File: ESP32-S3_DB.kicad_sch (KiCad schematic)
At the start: 0 parts

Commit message: Started ESP routing
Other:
- sheet CAN TRANSCEIVER ports: added CAN_N, CAN_P; removed CAN_H, CAN_L
- sheet ESP32-S3 ports: added none; removed GPIO15, GPIO16
- sheet EXTERNAL CONNECTORS ports: added CAN_N, CAN_P, RS485_N, RS485_P; removed CAN_H, CAN_L, GPIO15, GPIO16, RS-485_A, RS-485_B
- sheet RS_485 ports: added RS485_N, RS485_P; removed RS_485_A, RS_485_B
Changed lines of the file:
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@@
     (stroke (width 0.5) (type default) (color 0 0 255 1))
-  )
-  (wire (pts (xy 259.715 123.825) (xy 276.225 123.825))
-    (stroke (width 0.5) (type default) (color 72 0 72 1))
   )
   (wire (pts (xy 199.39 85.725) (xy 220.345 85.725))
@@
     (stroke (width 0.5) (type default) (color 0 0 255 1))
   )
-  (wire (pts (xy 165.735 110.49) (xy 174.625 110.49))
-    (stroke (width 0.5) (type default) (color 72 0 72 1))
-  )
   (polyline (pts (xy 88.9 147.32) (xy 88.9 61.595))
     (stroke (width 0.4) (type dash) (color 0 0 0 1))
   )
-  (wire (pts (xy 259.715 121.285) (xy 276.225 121.285))
-    (stroke (width 0.5) (type default) (color 72 0 72 1))
-  )
   (wire (pts (xy 212.725 37.465) (xy 227.965 37.465))
     (stroke (width 0.5) (type default) (color 204 102 0 1))
@@
   )
   (wire (pts (xy 220.345 93.345) (xy 199.39 93.345))
-    (stroke (width 0.5) (type default) (color 72 0 72 1))
-  )
-  (wire (pts (xy 165.735 107.95) (xy 174.625 107.95))
     (stroke (width 0.5) (type default) (color 72 0 72 1))
   )
@@
     (effects (font (size 1.27 1.27) bold (color 72 0 72 1)) (justify left bottom))
   )
-  (label "RS_485_B" (at 276.225 83.185 180) (fields_autoplaced)
+  (label "RS485_N" (at 276.225 83.185 180) (fields_autoplaced)
     (effects (font (size 1.27 1.27) bold (color 0 0 0 1)) (justify right bottom))
   )
@@
     (effects (font (size 1.27 1.27) bold (color 72 0 72 1)) (justify left bottom))
   )
-  (label "GPIO16" (at 174.625 107.95 180) (fields_autoplaced)
-    (effects (font (size 1.27 1.27) bold (color 72 0 72 1)) (justify right bottom))
-  )
   (label "GPIO3" (at 276.225 106.045 180) (fields_autoplaced)
     (effects (font (size 1.27 1.27) bold (color 72 0 72 1)) (justify right bottom))
@@
     (effects (font (size 1.27 1.27) bold (color 132 132 0 1)) (justify left bottom))
   )
-  (label "GPIO16" (at 276.225 123.825 180) (fields_autoplaced)
-    (effects (font (size 1.27 1.27) bold (color 72 0 72 1)) (justify right bottom))
-  )
   (label "U2U_CONN_TX" (at 95.885 174.625 180) (fields_autoplaced)
     (effects (font (size 1.27 1.27) (thickness 0.254) bold (color 0 0 255 1)) (justify right bottom))
@@
     (effects (font (size 1.27 1.27) bold (color 132 0 0 1)) (justify left bottom))
   )
-  (label "RS_485_B" (at 23.495 84.455 0) (fields_autoplaced)
+  (label "RS485_N" (at 23.495 84.455 0) (fields_autoplaced)
     (effects (font (size 1.27 1.27) bold (color 0 0 0 1)) (justify left bottom))
   )
@@
     (effects (font (size 1.27 1.27) bold (color 72 0 72 1)) (justify right bottom))
   )
-  (label "RS_485_A" (at 23.495 81.915 0) (fields_autoplaced)
+  (label "RS485_P" (at 23.495 81.915 0) (fields_autoplaced)
     (effects (font (size 1.27 1.27) bold (color 0 0 0 1)) (justify left bottom))
   )
@@
   (label "R4_~{RE}_DE" (at 199.39 111.125 0) (fields_autoplaced)
     (effects (font (size 1.27 1.27) bold (color 72 0 72 1)) (justify left bottom))
-  )
-  (label "GPIO15" (at 174.625 110.49 180) (fields_autoplaced)
-    (effects (font (size 1.27 1.27) bold (color 72 0 72 1)) (justify right bottom))
   )
   (label "BOOT" (at 97.155 114.3 0) (fields_autoplaced)
@@
     (effects (font (size 1.27 1.27) bold (color 0 0 255 1)) (justify left bottom))
   )
-  (label "CAN_H" (at 276.225 85.725 180) (fields_autoplaced)
+  (label "CAN_P" (at 276.225 85.725 180) (fields_autoplaced)
     (effects (font (size 1.27 1.27) bold (color 0 0 0 1)) (justify right bottom))
   )
-  (label "CAN_L" (at 276.225 88.265 180) (fields_autoplaced)
+  (label "CAN_N" (at 276.225 88.265 180) (fields_autoplaced)
     (effects (font (size 1.27 1.27) bold (color 0 0 0 1)) (justify right bottom))
   )
@@
     (effects (font (size 1.27 1.27) bold (color 0 0 255 1)) (justify right bottom))
   )
-  (label "RS_485_A" (at 276.225 80.645 180) (fields_autoplaced)
+  (label "RS485_P" (at 276.225 80.645 180) (fields_autoplaced)
     (effects (font (size 1.27 1.27) bold (color 0 0 0 1)) (justify right bottom))
   )
@@
     (effects (font (size 1.27 1.27) bold (color 0 194 0 1)) (justify left bottom))
   )
-  (label "CAN_H" (at 30.48 125.095 0) (fields_autoplaced)
+  (label "CAN_P" (at 30.48 125.095 0) (fields_autoplaced)
     (effects (font (size 1.27 1.27) bold (color 0 0 0 1)) (justify left bottom))
-  )
-  (label "GPIO15" (at 276.225 121.285 180) (fields_autoplaced)
-    (effects (font (size 1.27 1.27) bold (color 72 0 72 1)) (justify right bottom))
   )
   (label "U2U_TXD" (at 181.61 34.925 180) (fields_autoplaced)
@@
     (effects (font (size 1.27 1.27) bold (color 72 0 72 1)) (justify right bottom))
   )
-  (label "CAN_L" (at 30.48 122.555 0) (fields_autoplaced)
+  (label "CAN_N" (at 30.48 122.555 0) (fields_autoplaced)
     (effects (font (size 1.27 1.27) bold (color 0 0 0 1)) (justify left bottom))
   )
@@
       (effects (font (size 1.27 1.27)) (justify left top) hide)
     )
-    (pin "CAN_L" input (at 40.005 122.555 180)
+    (pin "CAN_N" input (at 40.005 122.555 180)
       (effects (font (size 1.27 1.27) (thickness 0.254) bold (color 0 0 0 1)) (justify left))
     )
@@
       (effects (font (size 1.27 1.27) (thickness 0.254) bold (color 255 0 0 1)) (justify right))
     )
-    (pin "CAN_H" input (at 40.005 125.095 180)
+    (pin "CAN_P" input (at 40.005 125.095 180)
       (effects (font (size 1.27 1.27) (thickness 0.254) bold (color 0 0 0 1)) (justify left))
     )
@@
       (effects (font (size 1.27 1.27) (thickness 0.254) bold (color 0 194 0 1)) (justify left))
     )
-    (pin "RS_485_A" bidirectional (at 40.005 81.915 180)
+    (pin "RS485_P" bidirectional (at 40.005 81.915 180)
       (effects (font (size 1.27 1.27) (thickness 0.254) bold (color 0 0 0 1)) (justify left))
     )
-    (pin "RS_485_B" bidirectional (at 40.005 84.455 180)
+    (pin "RS485_N" bidirectional (at 40.005 84.455 180)
       (effects (font (size 1.27 1.27) (thickness 0.254) bold (color 0 0 0 1)) (justify left))
     )
@@
       (effects (font (size 1.27 1.27) (thickness 0.254) bold (color 72 0 72 1)) (justify right))
     )
-    (pin "GPIO16" output (at 165.735 107.95 0)
-      (effects (font (size 1.27 1.27) (thickness 0.254) bold (color 72 0 72 1)) (justify right))
-    )
-    (pin "GPIO15" output (at 165.735 110.49 0)
-      (effects (font (size 1.27 1.27) (thickness 0.254) bold (color 72 0 72 1)) (justify right))
-    )
     (pin "GPIO14" output (at 165.735 113.03 0)
       (effects (font (size 1.27 1.27) (thickness 0.254) bold (color 72 0 72 1)) (justify right))
@@
       (effects (font (size 1.27 1.27)) (justify left top) hide)
     )
-    (pin "RS-485_A" input (at 259.715 80.645 0)
+    (pin "RS485_P" input (at 259.715 80.645 0)
       (effects (font (size 1.27 1.27) (thickness 0.254) bold (color 0 0 0 1)) (justify right))
     )
-    (pin "RS-485_B" input (at 259.715 83.185 0)
+    (pin "RS485_N" input (at 259.715 83.185 0)
       (effects (font (size 1.27 1.27) (thickness 0.254) bold (color 0 0 0 1)) (justify right))
     )
-    (pin "CAN_H" input (at 259.715 85.725 0)
+    (pin "CAN_P" input (at 259.715 85.725 0)
       (effects (font (size 1.27 1.27) (thickness 0.254) bold (color 0 0 0 1)) (justify right))
     )
-    (pin "CAN_L" input (at 259.715 88.265 0)
+    (pin "CAN_N" input (at 259.715 88.265 0)
       (effects (font (size 1.27 1.27) (thickness 0.254) bold (color 0 0 0 1)) (justify right))
     )
@@
       (effects (font (size 1.27 1.27) (thickness 0.254) bold (color 72 0 0 1)) (justify right))
     )
-    (pin "GPIO15" input (at 259.715 121.285 0)
-      (effects (font (size 1.27 1.27) (thickness 0.254) bold (color 72 0 0 1)) (justify right))
-    )
-    (pin "GPIO16" input (at 259.715 123.825 0)
-      (effects (font (size 1.27 1.27) (thickness 0.254) bold (color 72 0 0 1)) (justify right))
-    )

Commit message: Finished routing
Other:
- sheet ESP32-S3 ports: added GPIO45, GPIO46, RS-485_RX/GPIO34, RS-485_TX/GPIO33; removed GPIO33, GPIO34, RS-485_RX/GPIO46, RS-485_TX/GPIO45
- sheet EXTERNAL CONNECTORS ports: added GPIO45, GPIO46, RS-485_RX/GPIO34, RS-485_TX/GPIO33; removed GPIO33, GPIO34, RS-485_RX/GPIO46, RS-485_TX/GPIO45
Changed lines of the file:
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@@
     (effects (font (size 1.27 1.27) bold (color 0 194 0 1)) (justify right bottom))
   )
-  (label "GPIO33" (at 135.89 132.715 90) (fields_autoplaced)
+  (label "GPIO45" (at 135.89 132.715 90) (fields_autoplaced)
     (effects (font (size 1.27 1.27) bold (color 72 0 72 1)) (justify left bottom))
   )
@@
     (effects (font (size 1.27 1.27) bold (color 72 0 72 1)) (justify right bottom))
   )
-  (label "GPIO33" (at 199.39 116.205 0) (fields_autoplaced)
+  (label "GPIO45" (at 199.39 116.205 0) (fields_autoplaced)
     (effects (font (size 1.27 1.27) bold (color 72 0 72 1)) (justify left bottom))
   )
@@
     (effects (font (size 1.27 1.27) bold (color 0 0 255 1)) (justify left bottom))
   )
-  (label "RS-485_TX{slash}GPIO45" (at 95.885 169.545 180) (fields_autoplaced)
-    (effects (font (size 1.27 1.27) bold (color 0 0 255 1)) (justify right bottom))
-  )
-  (label "RS-485_TX{slash}GPIO45" (at 199.39 80.645 0) (fields_autoplaced)
+  (label "RS-485_RX{slash}GPIO34" (at 95.885 169.545 180) (fields_autoplaced)
+    (effects (font (size 1.27 1.27) bold (color 0 0 255 1)) (justify right bottom))
+  )
+  (label "RS-485_TX{slash}GPIO33" (at 199.39 80.645 0) (fields_autoplaced)
     (effects (font (size 1.27 1.27) bold (color 0 0 255 1)) (justify left bottom))
   )
@@
     (effects (font (size 1.27 1.27) bold (color 72 0 72 1)) (justify left bottom))
   )
-  (label "RS-485_TX{slash}GPIO45" (at 97.155 93.98 0) (fields_autoplaced)
+  (label "RS-485_TX{slash}GPIO33" (at 97.155 93.98 0) (fields_autoplaced)
     (effects (font (size 1.27 1.27) bold (color 0 0 255 1)) (justify left bottom))
   )
@@
     (effects (font (size 1.27 1.27) bold (color 204 102 0 1)) (justify right bottom))
   )
-  (label "RS-485_RX{slash}GPIO46" (at 199.39 83.185 0) (fields_autoplaced)
+  (label "RS-485_RX{slash}GPIO34" (at 199.39 83.185 0) (fields_autoplaced)
     (effects (font (size 1.27 1.27) bold (color 0 0 255 1)) (justify left bottom))
   )
@@
     (effects (font (size 1.27 1.27) bold (color 0 0 0 1)) (justify left bottom))
   )
-  (label "RS-485_RX{slash}GPIO46" (at 95.885 172.085 180) (fields_autoplaced)
+  (label "RS-485_TX{slash}GPIO33" (at 95.885 172.085 180) (fields_autoplaced)
     (effects (font (size 1.27 1.27) bold (color 0 0 255 1)) (justify right bottom))
   )
@@
     (effects (font (size 1.27 1.27) (thickness 0.254) bold (color 204 102 0 1)) (justify left bottom))
   )
-  (label "GPIO34" (at 138.43 132.715 90) (fields_autoplaced)
+  (label "GPIO46" (at 138.43 132.715 90) (fields_autoplaced)
     (effects (font (size 1.27 1.27) bold (color 72 0 72 1)) (justify left bottom))
   )
@@
     (effects (font (size 1.27 1.27) bold (color 72 0 72 1)) (justify left bottom))
   )
-  (label "RS-485_RX{slash}GPIO46" (at 97.155 91.44 0) (fields_autoplaced)
+  (label "RS-485_RX{slash}GPIO34" (at 97.155 91.44 0) (fields_autoplaced)
     (effects (font (size 1.27 1.27) bold (color 0 0 255 1)) (justify left bottom))
   )
@@
     (effects (font (size 1.27 1.27) bold (color 0 0 255 1)) (justify right bottom))
   )
-  (label "GPIO34" (at 199.39 113.665 0) (fields_autoplaced)
+  (label "GPIO46" (at 199.39 113.665 0) (fields_autoplaced)
     (effects (font (size 1.27 1.27) bold (color 72 0 72 1)) (justify left bottom))
   )
@@
       (effects (font (size 1.27 1.27) (thickness 0.254) bold (color 0 0 255 1)) (justify left))
     )
-    (pin "RS-485_TX{slash}GPIO45" output (at 116.84 93.98 180)
-      (effects (font (size 1.27 1.27) (thickness 0.254) bold (color 0 0 255 1)) (justify left))
-    )
-    (pin "RS-485_RX{slash}GPIO46" input (at 116.84 91.44 180)
+    (pin "RS-485_TX{slash}GPIO33" output (at 116.84 93.98 180)
+      (effects (font (size 1.27 1.27) (thickness 0.254) bold (color 0 0 255 1)) (justify left))
+    )
+    (pin "RS-485_RX{slash}GPIO34" input (at 116.84 91.44 180)
       (effects (font (size 1.27 1.27) (thickness 0.254) bold (color 0 0 255 1)) (justify left))
     )
@@
       (effects (font (size 1.27 1.27) (thickness 0.254) bold (color 72 0 72 1)) (justify left))
     )
-    (pin "GPIO34" output (at 138.43 123.825 270)
-      (effects (font (size 1.27 1.27) (thickness 0.254) bold (color 72 0 72 1)) (justify left))
-    )
-    (pin "GPIO33" output (at 135.89 123.825 270)
+    (pin "GPIO46" output (at 138.43 123.825 270)
+      (effects (font (size 1.27 1.27) (thickness 0.254) bold (color 72 0 72 1)) (justify left))
+    )
+    (pin "GPIO45" output (at 135.89 123.825 270)
       (effects (font (size 1.27 1.27) (thickness 0.254) bold (color 72 0 72 1)) (justify left))
     )
@@
       (effects (font (size 1.27 1.27) (thickness 0.254) bold (color 0 0 255 1)) (justify right))
     )
-    (pin "RS-485_TX{slash}GPIO45" output (at 220.345 80.645 180)
-      (effects (font (size 1.27 1.27) (thickness 0.254) bold (color 0 0 255 1)) (justify left))
-    )
-    (pin "RS-485_RX{slash}GPIO46" output (at 220.345 83.185 180)
+    (pin "RS-485_TX{slash}GPIO33" output (at 220.345 80.645 180)
+      (effects (font (size 1.27 1.27) (thickness 0.254) bold (color 0 0 255 1)) (justify left))
+    )
+    (pin "RS-485_RX{slash}GPIO34" output (at 220.345 83.185 180)
       (effects (font (size 1.27 1.27) (thickness 0.254) bold (color 0 0 255 1)) (justify left))
     )
@@
       (effects (font (size 1.27 1.27) (thickness 0.254) bold (color 72 0 0 1)) (justify left))
     )
-    (pin "GPIO33" input (at 220.345 116.205 180)
+    (pin "GPIO45" input (at 220.345 116.205 180)
       (effects (font (size 1.27 1.27) (thickness 0.254) bold (color 72 0 0 1)) (justify left))
     )
-    (pin "GPIO34" input (at 220.345 113.665 180)
+    (pin "GPIO46" input (at 220.345 113.665 180)
       (effects (font (size 1.27 1.27) (thickness 0.254) bold (color 72 0 0 1)) (justify left))
     )

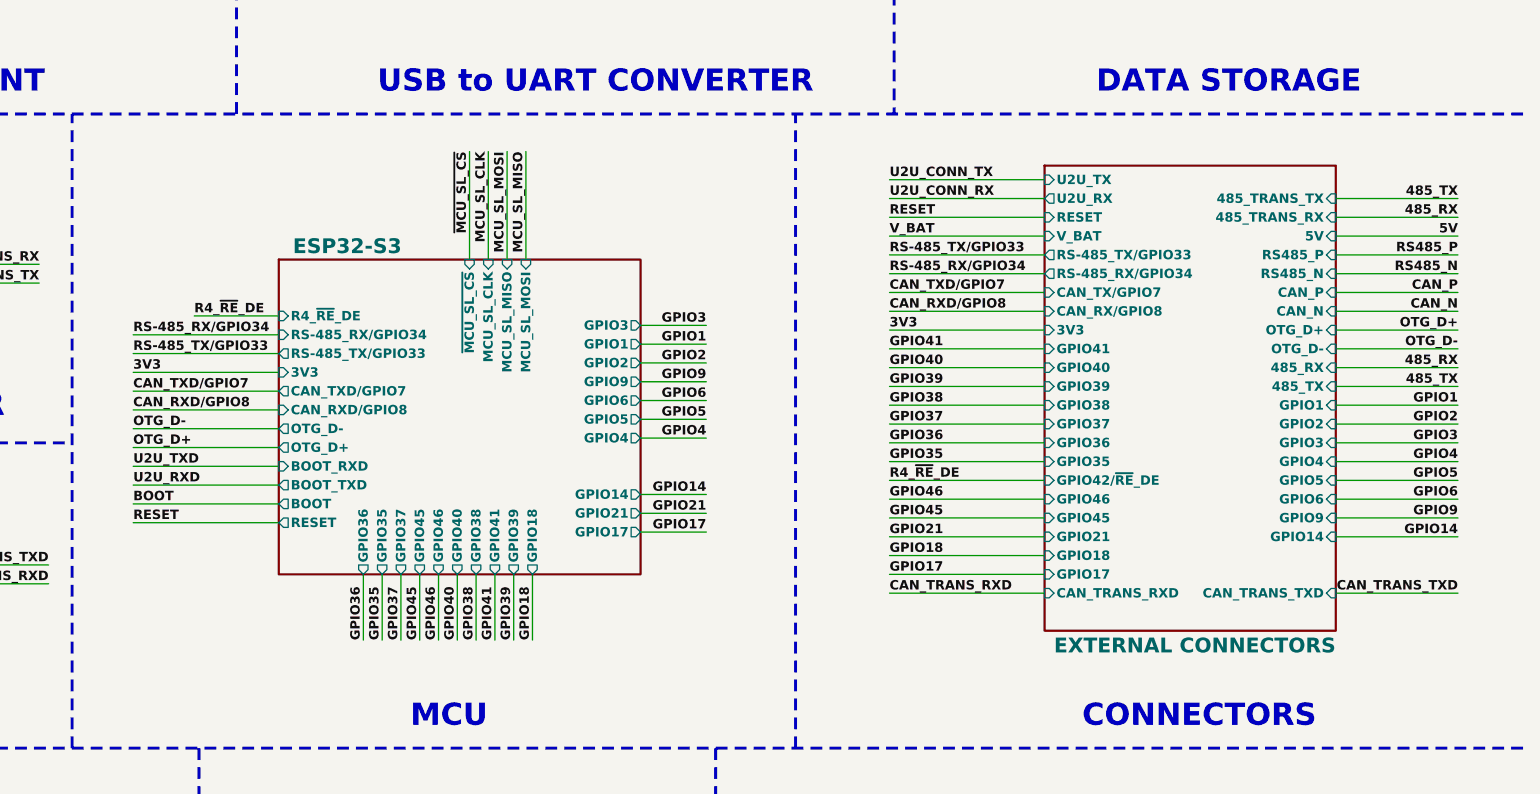
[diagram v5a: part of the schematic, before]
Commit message: Added selection jumper block diagram and solved DRC errors
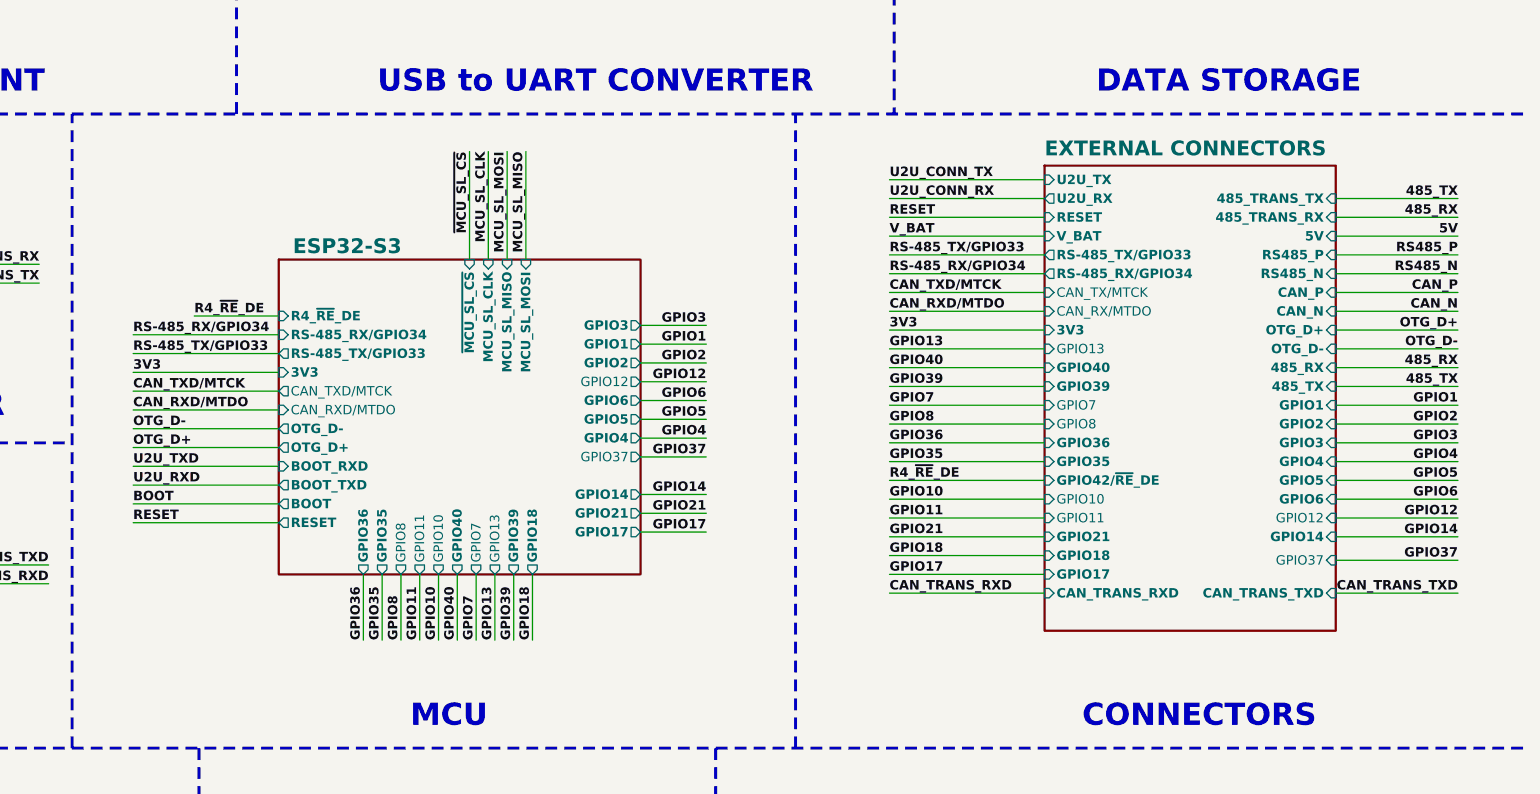
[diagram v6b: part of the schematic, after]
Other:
- sheet ESP32-S3 ports: added CAN_RXD/MTDO, CAN_TXD/MTCK, GPIO10, GPIO11, GPIO12, GPIO13, GPIO7, GPIO8; removed CAN_RXD/GPIO8, CAN_TXD/GPIO7, GPIO38, GPIO41, GPIO45, GPIO46, GPIO9
- sheet EXTERNAL CONNECTORS ports: added CAN_RX/MTDO, CAN_TX/MTCK, GPIO10, GPIO11, GPIO12, GPIO13, GPIO7, GPIO8; removed CAN_RX/GPIO8, CAN_TX/GPIO7, GPIO38, GPIO41, GPIO45, GPIO46, GPIO9

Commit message: Added HW-Tinkerers logo and supporting graphics
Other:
- company: (none) -> HW-TINKERERS (hw.tinkerers@gmail.com)
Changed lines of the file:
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@@
   (title_block
     (title "HARDWARE TINKERERS ESP32-S3 DB")
+    (date "22/08/2023")
     (rev "1.0.0")
+    (company "HW-TINKERERS (hw.tinkerers@gmail.com)")
+    (comment 1 "Email: bhandarkasrishtikr111@gmail.com")
+    (comment 2 "Author: Srishtik Bhandarkar")
+    (comment 3 "Email: vaibhavkhatri00@gmail.com")
+    (comment 4 "Author: Vaibhav Khatri")
   )
   (wire (pts (xy 143.51 39.37) (xy 132.715 39.37))
